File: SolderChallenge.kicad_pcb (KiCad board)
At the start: 2 copper layers, 50 x 100 mm, 41 parts, among them Q1 MOS_N, Q2 MOS_N, Q3 MOS_N, Q4 MOS_N_x2, U1 555, U2 555, U3 555

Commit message: Add name, rev and github URL to back silkscreen
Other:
- board text added: "Iain Chalmers V0.2 https://github.com/icchalmers/SolderChallenge"
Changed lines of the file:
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@@
   (general
     (thickness 1.6)
-    (drawings 54)
+    (drawings 55)
     (tracks 255)
     (zones 0)
@@
     )
   )
+  (gr_text "Iain Chalmers\nV0.2\nhttps://github.com/icchalmers/SolderChallenge" (at 74.7 56.2) (layer B.SilkS)
+    (effects (font (size 1.2 1.2) (thickness 0.2)) (justify mirror))
+  )
   (gr_text "Press 9V battery\non pads to display score" (at 54.25 76 90) (layer F.SilkS)

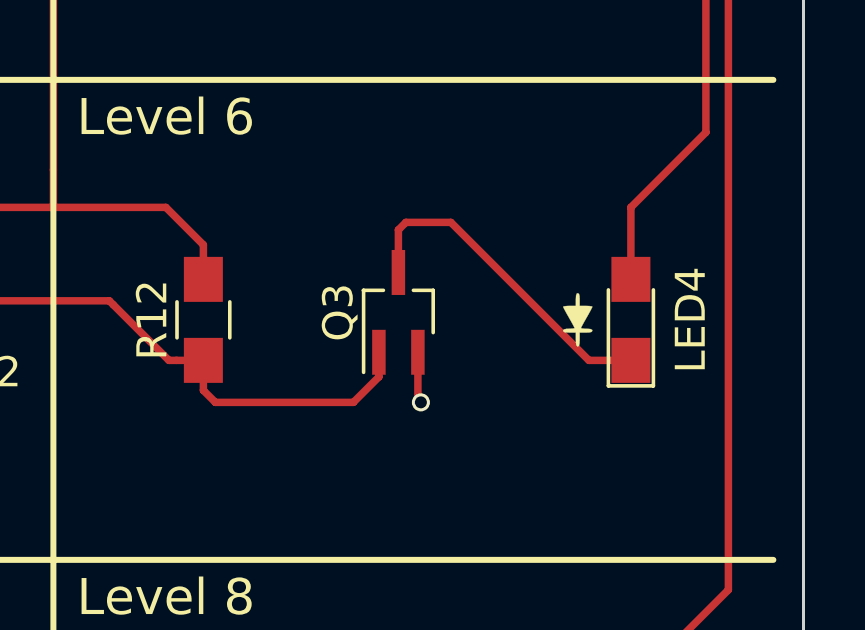
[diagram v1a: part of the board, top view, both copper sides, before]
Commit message: Change Q3 to SOT-23 in place of SOT-323. The difference is that the Q3 footprint uses the recommended solder footprint, whereas Q2 uses the KiCAD hand solder footprint. Should be a good example of using the right footprint depending on the situation
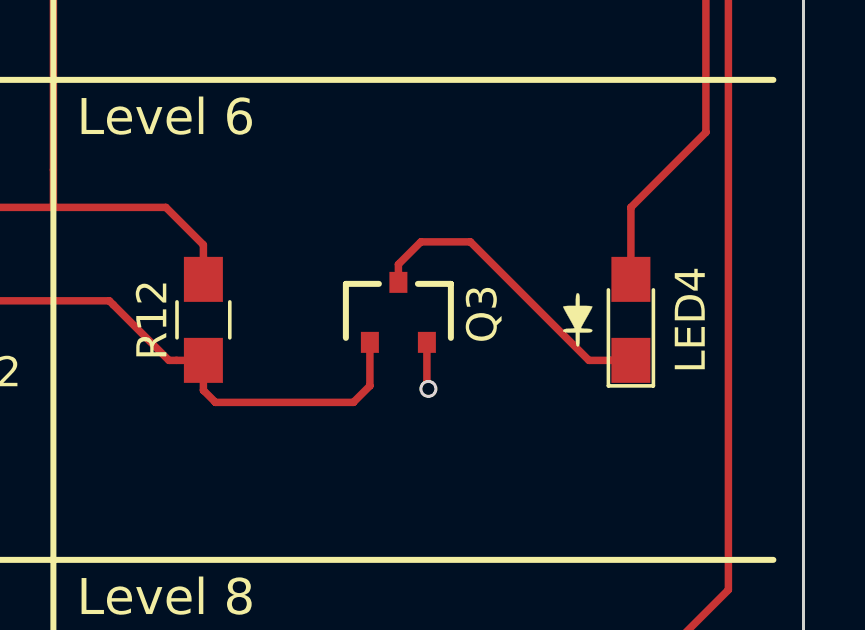
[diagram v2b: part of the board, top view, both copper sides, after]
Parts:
- Q3: footprint SolderChallenge:SOT-323_SC-70_GSD_Handsoldering -> SolderChallenge:SOT-23_GSD_Nexperia_TO-236AB
- turned Q3 to 180 degrees
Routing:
- net Net-(LED4-Pad1): track 11.2 -> 10.3 mm
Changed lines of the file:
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@@
     (add_net VCC)
+  )
+  (module SolderChallenge:SOT-23_GSD_Nexperia_TO-236AB (layer F.Cu)
+    (at 86.5 115.75 180)
+    (descr "SOT-23, Standard")
+    (tags SOT-23)
+    (attr smd)
+    (fp_text reference Q3 (at -2.8 -0.05 90) (layer F.SilkS)
+      (effects (font (size 1 1) (thickness 0.15)))
+    )
+    (fp_text value MOS_N (at 0 2.5 180) (layer F.Fab)
+      (effects (font (size 1 1) (thickness 0.15)))
+    )
+    (fp_line (start 1.45 -0.85) (end 1.65 -0.85) (layer F.CrtYd) (width 0.2))
+    (fp_line (start 1.45 -1.5) (end 1.45 -0.85) (layer F.CrtYd) (width 0.2))
+    (fp_line (start -1.45 -0.85) (end -1.65 -0.85) (layer F.CrtYd) (width 0.2))
+    (fp_line (start -1.45 -1.5) (end -1.45 -0.85) (layer F.CrtYd) (width 0.2))
+    (fp_line (start -1.65 0.85) (end 1.65 0.85) (layer F.CrtYd) (width 0.2))
+    (fp_line (start 1.65 -0.85) (end 1.65 0.85) (layer F.CrtYd) (width 0.2))
+    (fp_line (start -1.45 -1.5) (end 1.45 -1.5) (layer F.CrtYd) (width 0.2))
+    (fp_line (start -1.65 -0.85) (end -1.65 0.85) (layer F.CrtYd) (width 0.2))
+    (fp_line (start 1.75 0.95) (end 0.65 0.95) (layer F.SilkS) (width 0.2))
+    (fp_line (start 1.75 -0.85) (end 1.75 0.95) (layer F.SilkS) (width 0.2))
+    (fp_line (start -1.75 0.95) (end -0.65 0.95) (layer F.SilkS) (width 0.2))
+    (fp_line (start -1.75 -0.85) (end -1.75 0.95) (layer F.SilkS) (width 0.2))
+    (fp_line (start -1.65 -0.85) (end -1.65 0.85) (layer F.Fab) (width 0.2))
+    (fp_line (start 1.65 -0.25) (end 1.65 0.85) (layer F.Fab) (width 0.2))
+    (fp_line (start -1.65 -0.85) (end 1.1 -0.85) (layer F.Fab) (width 0.2))
+    (fp_line (start -1.65 0.85) (end 1.65 0.85) (layer F.Fab) (width 0.2))
+    (fp_line (start 1.1 -0.85) (end 1.65 -0.25) (layer F.Fab) (width 0.2))
+    (pad D smd rect (at 0 1 180) (size 0.6 0.7) (layers F.Cu F.Paste F.Mask)
+      (net 12 "Net-(LED4-Pad1)") (solder_mask_margin 0.05) (solder_paste_margin -0.05))
+    (pad G smd rect (at 0.95 -1 180) (size 0.6 0.7) (layers F.Cu F.Paste F.Mask)
+      (net 22 "Net-(Q3-PadG)") (solder_mask_margin 0.05) (solder_paste_margin -0.05))
+    (pad S smd rect (at -0.95 -1 180) (size 0.6 0.7) (layers F.Cu F.Paste F.Mask)
+      (net 2 GND) (solder_mask_margin 0.05) (solder_paste_margin -0.05))
+    (model TO_SOT_Packages_SMD.3dshapes/SOT-23.wrl
+      (at (xyz 0 0 0))
+      (scale (xyz 1 1 1))
+      (rotate (xyz 0 0 90))
+    )
   )
   (module SolderChallenge:TSSOP-8_4.4x3mm_Pitch0.65mm (layer F.Cu)
@@
       (xy 15.738353 -1.07461)) (layer F.Mask) (width 0.01))
   )
-  (module SolderChallenge:SOT-323_SC-70_GSD_Handsoldering (layer F.Cu)
-    (at 86.5 115.75 90)
-    (descr "SOT-323, SC-70 Handsoldering")
-    (tags "SOT-323 SC-70 Handsoldering")
-    (attr smd)
-    (fp_text reference Q3 (at 0 -2 90) (layer F.SilkS)
-      (effects (font (size 1 1) (thickness 0.15)))
-    )
-    (fp_text value MOS_N (at 0 2.05 90) (layer F.Fab) hide
-      (effects (font (size 1 1) (thickness 0.15)))
-    )
-    (fp_text user %R (at 0 0 180) (layer F.Fab)
-      (effects (font (size 0.5 0.5) (thickness 0.075)))
-    )
-    (fp_line (start 0.735 0.5) (end 0.735 1.16) (layer F.SilkS) (width 0.12))
-    (fp_line (start 0.735 -1.17) (end 0.735 -0.5) (layer F.SilkS) (width 0.12))
-    (fp_line (start 2.4 1.3) (end -2.4 1.3) (layer F.CrtYd) (width 0.05))
-    (fp_line (start 2.4 -1.3) (end 2.4 1.3) (layer F.CrtYd) (width 0.05))
-    (fp_line (start -2.4 -1.3) (end 2.4 -1.3) (layer F.CrtYd) (width 0.05))
-    (fp_line (start -2.4 1.3) (end -2.4 -1.3) (layer F.CrtYd) (width 0.05))
-    (fp_line (start 0.735 -1.16) (end -2 -1.16) (layer F.SilkS) (width 0.12))
-    (fp_line (start -0.675 1.16) (end 0.735 1.16) (layer F.SilkS) (width 0.12))
-    (fp_line (start 0.675 -1.1) (end -0.175 -1.1) (layer F.Fab) (width 0.1))
-    (fp_line (start -0.675 -0.6) (end -0.675 1.1) (layer F.Fab) (width 0.1))
-    (fp_line (start 0.675 -1.1) (end 0.675 1.1) (layer F.Fab) (width 0.1))
-    (fp_line (start 0.675 1.1) (end -0.675 1.1) (layer F.Fab) (width 0.1))
-    (fp_line (start -0.175 -1.1) (end -0.675 -0.6) (layer F.Fab) (width 0.1))
-    (pad G smd rect (at -1.33 -0.65) (size 0.45 1.5) (layers F.Cu F.Paste F.Mask)
-      (net 22 "Net-(Q3-PadG)"))
-    (pad S smd rect (at -1.33 0.65) (size 0.45 1.5) (layers F.Cu F.Paste F.Mask)
-      (net 2 GND))
-    (pad D smd rect (at 1.33 0) (size 0.45 1.5) (layers F.Cu F.Paste F.Mask)
-      (net 12 "Net-(LED4-Pad1)"))
-    (model ${KISYS3DMOD}/TO_SOT_Packages_SMD.3dshapes/SOT-323_SC-70.wrl
-      (at (xyz 0 0 0))
-      (scale (xyz 1 1 1))
-      (rotate (xyz 0 0 0))
-    )
-  )
   (module SolderChallenge:SOT-23_GSD_Handsoldering (layer F.Cu)
     (at 87.075 100 90)
@@
   (segment (start 71.655 117.905) (end 72 118.25) (width 0.25) (layer F.Cu) (net 2))
   (segment (start 72 118.25) (end 72 118.75) (width 0.25) (layer F.Cu) (net 2))
-  (segment (start 87.15 117.08) (end 87.15 118.65) (width 0.25) (layer F.Cu) (net 2))
-  (segment (start 87.15 118.65) (end 87.25 118.75) (width 0.25) (layer F.Cu) (net 2))
-  (via (at 87.25 118.75) (size 0.6) (drill 0.4) (layers F.Cu B.Cu) (net 2))
   (segment (start 70.95 132.975) (end 71.975 132.975) (width 0.25) (layer F.Cu) (net 2))
   (segment (start 71.975 132.975) (end 72.5 133.5) (width 0.25) (layer F.Cu) (net 2))
@@
   (segment (start 88.025 103.225) (end 88 103.25) (width 0.25) (layer F.Cu) (net 2))
   (via (at 88 103.25) (size 0.6) (drill 0.4) (layers F.Cu B.Cu) (net 2))
+  (via (at 87.5 118.3) (size 0.6) (drill 0.4) (layers F.Cu B.Cu) (net 2))
+  (segment (start 87.45 116.75) (end 87.45 118.25) (width 0.25) (layer F.Cu) (net 2))
+  (segment (start 87.45 118.25) (end 87.5 118.3) (width 0.25) (layer F.Cu) (net 2))
   (segment (start 59.08 98.72) (end 61.62 101.26) (width 0.25) (layer B.Cu) (net 3))
   (segment (start 61.62 101.26) (end 66.7 101.26) (width 0.25) (layer B.Cu) (net 3))
@@
   (via (at 94.25 96.25) (size 0.6) (drill 0.4) (layers F.Cu B.Cu) (net 11))
   (segment (start 76.38 77.5) (end 76.38 83.88) (width 0.25) (layer B.Cu) (net 11))
-  (segment (start 86.5 114.42) (end 86.5 113) (width 0.25) (layer F.Cu) (net 12))
-  (segment (start 86.5 113) (end 86.75 112.75) (width 0.25) (layer F.Cu) (net 12))
-  (segment (start 86.75 112.75) (end 88.25 112.75) (width 0.25) (layer F.Cu) (net 12))
-  (segment (start 88.25 112.75) (end 92.85 117.35) (width 0.25) (layer F.Cu) (net 12))
   (segment (start 92.85 117.35) (end 94.25 117.35) (width 0.25) (layer F.Cu) (net 12))
+  (segment (start 88.9 113.4) (end 92.85 117.35) (width 0.25) (layer F.Cu) (net 12))
+  (segment (start 87.25 113.4) (end 88.9 113.4) (width 0.25) (layer F.Cu) (net 12))
+  (segment (start 86.5 114.15) (end 87.25 113.4) (width 0.25) (layer F.Cu) (net 12))
+  (segment (start 86.5 114.75) (end 86.5 114.15) (width 0.25) (layer F.Cu) (net 12))
   (segment (start 98 73.5) (end 98 74.75) (width 0.25) (layer F.Cu) (net 13))
   (segment (start 98 74.75) (end 96.75 76) (width 0.25) (layer F.Cu) (net 13))
@@
   (segment (start 80.4 118.75) (end 85 118.75) (width 0.25) (layer F.Cu) (net 22))
   (segment (start 80 118.35) (end 80.4 118.75) (width 0.25) (layer F.Cu) (net 22))
-  (segment (start 85 118.75) (end 85.85 117.9) (width 0.25) (layer F.Cu) (net 22))
-  (segment (start 85.85 117.9) (end 85.85 117.08) (width 0.25) (layer F.Cu) (net 22))
   (segment (start 77 115.5) (end 78.85 117.35) (width 0.25) (layer F.Cu) (net 22))
   (segment (start 78.85 117.35) (end 79.1 117.35) (width 0.25) (layer F.Cu) (net 22))
   (segment (start 79.1 117.35) (end 80 117.35) (width 0.25) (layer F.Cu) (net 22))
+  (segment (start 85.55 118.2) (end 85 118.75) (width 0.25) (layer F.Cu) (net 22))
+  (segment (start 85.55 116.75) (end 85.55 118.2) (width 0.25) (layer F.Cu) (net 22))
   (segment (start 58.25 133.35) (end 61.75 133.35) (width 0.25) (layer F.Cu) (net 23))
   (segment (start 61.75 133.35) (end 62.65 133.35) (width 0.25) (layer F.Cu) (net 23))

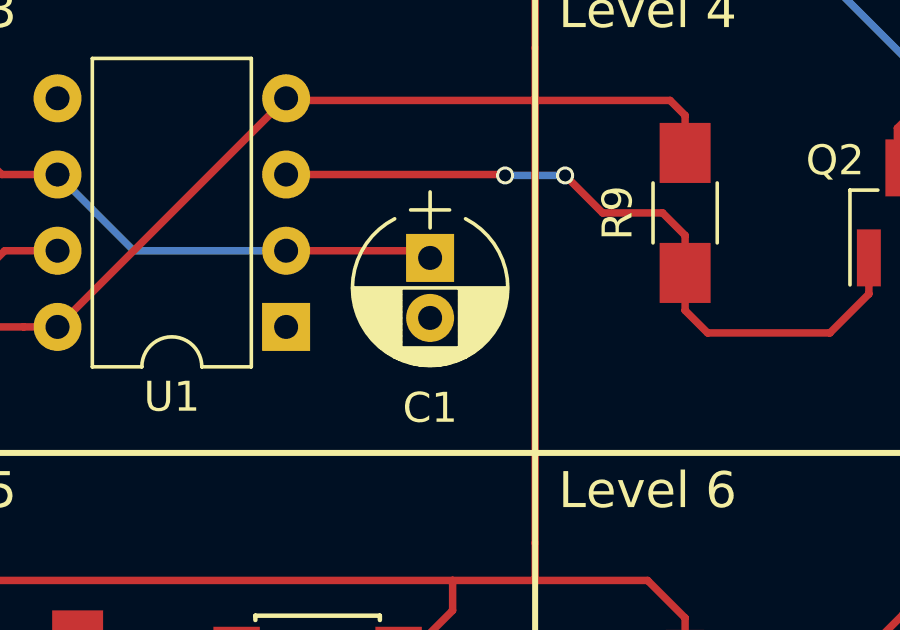
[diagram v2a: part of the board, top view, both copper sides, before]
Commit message: Change C1 to non polarised. Pops would have been fun if people soldered it in round the wrong way, but health and safety prevails over fun :(
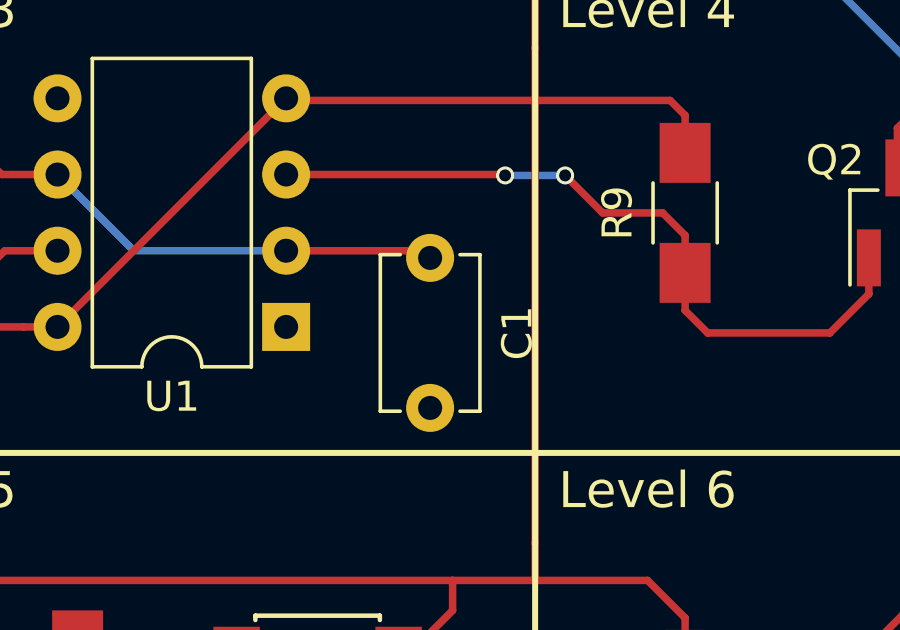
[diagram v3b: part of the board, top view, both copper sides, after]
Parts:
- C1: footprint SolderChallenge:CP_Radial_D5.0mm_P2.00mm -> SolderChallenge:C_Disc_D5.1mm_W3.2mm_P5.00mm

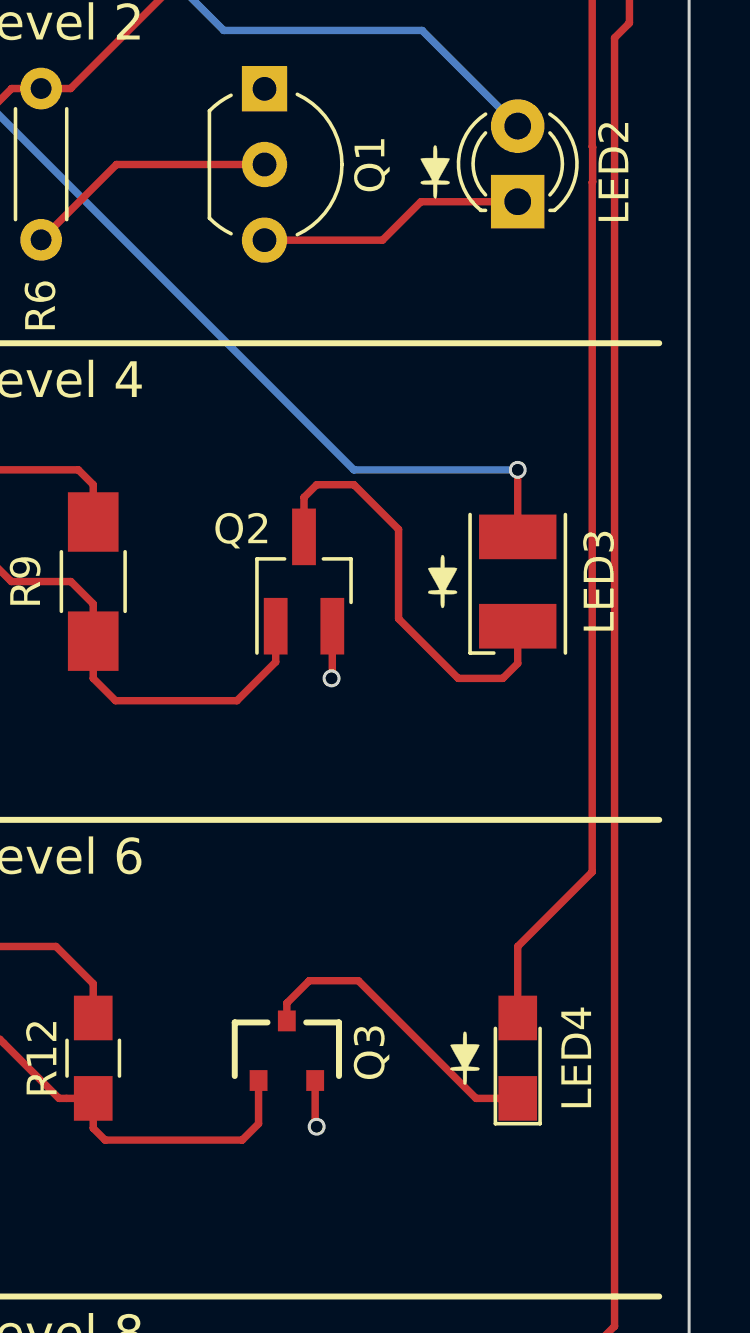
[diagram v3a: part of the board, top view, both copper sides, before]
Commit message: Switch orientation of one LED to force people to think about orientation. This is to make people more orientation aware without risking an exploding electrolytic in the face
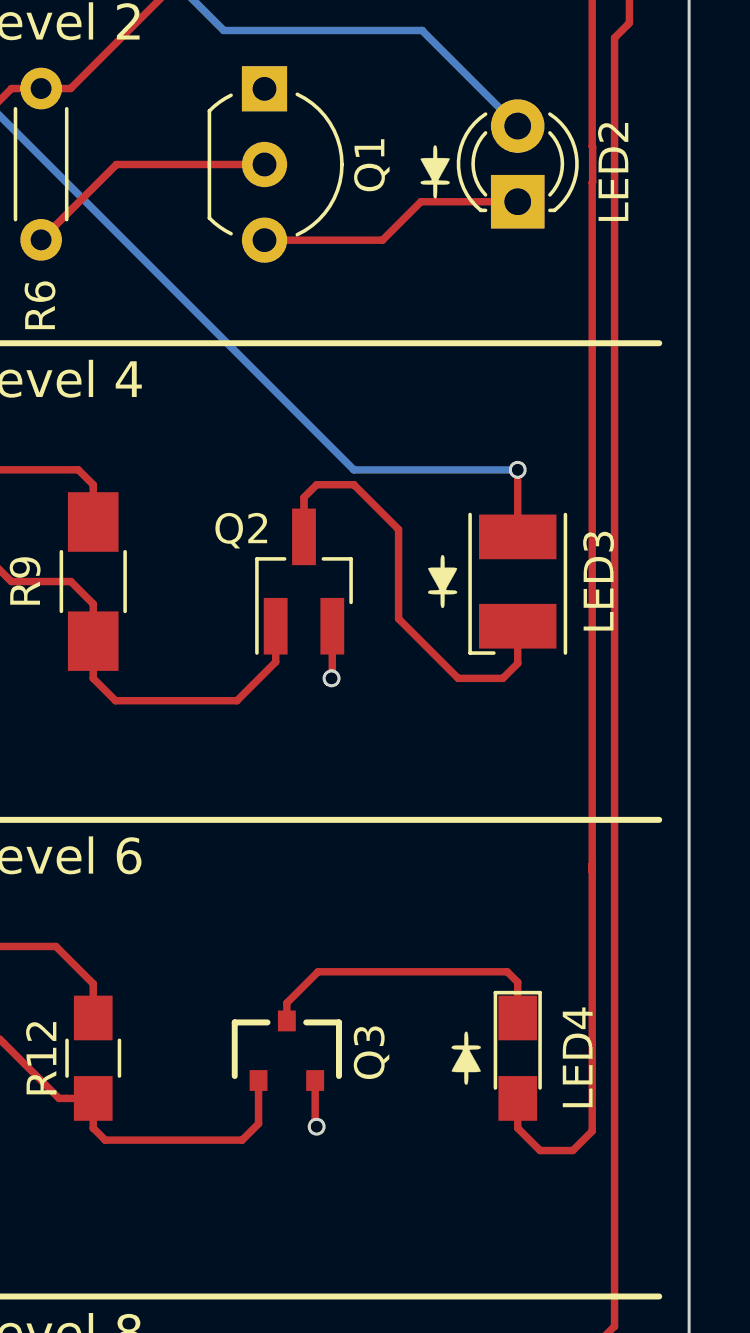
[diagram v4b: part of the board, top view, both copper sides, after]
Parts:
- turned G*** to 90 degrees
- turned LED4 to 270 degrees
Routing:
- net LED4_Vcc: track 42.7 -> 49.8 mm
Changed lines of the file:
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@@
     (thickness 1.6)
     (drawings 55)
-    (tracks 255)
+    (tracks 259)
     (zones 0)
     (modules 41)
@@
   )
   (module SolderChallenge:0803_diode_silk (layer F.Cu)
-    (at 92.5 116 270)
-    (fp_text reference G*** (at 0 0 270) (layer F.SilkS) hide
+    (at 92.5 116 90)
+    (fp_text reference G*** (at 0 0 90) (layer F.SilkS) hide
       (effects (font (size 1.524 1.524) (thickness 0.3)))
     )
-    (fp_text value LOGO (at 0.75 0 270) (layer F.SilkS) hide
+    (fp_text value LOGO (at 0.75 0 90) (layer F.SilkS) hide
       (effects (font (size 1.524 1.524) (thickness 0.3)))
     )
@@
   )
   (module SolderChallenge:LED_0805_HandSoldering (layer F.Cu)
-    (at 94.25 116 90)
+    (at 94.25 116 270)
     (descr "Resistor SMD 0805, hand soldering")
     (tags "resistor 0805")
     (attr smd)
-    (fp_text reference LED4 (at 0 2 90) (layer F.SilkS)
-      (effects (font (size 1 1) (thickness 0.15)))
-    )
-    (fp_text value LED (at 0 1.75 90) (layer F.Fab)
+    (fp_text reference LED4 (at 0 -2.05 270) (layer F.SilkS)
+      (effects (font (size 1 1) (thickness 0.15)))
+    )
+    (fp_text value LED (at 0 1.75 270) (layer F.Fab)
       (effects (font (size 1 1) (thickness 0.15)))
     )
@@
     (fp_line (start 2.35 0.9) (end -2.35 0.9) (layer F.CrtYd) (width 0.05))
     (fp_line (start -2.2 -0.75) (end -2.2 0.75) (layer F.SilkS) (width 0.12))
-    (pad 1 smd rect (at -1.35 0 90) (size 1.5 1.3) (layers F.Cu F.Paste F.Mask)
+    (pad 1 smd rect (at -1.35 0 270) (size 1.5 1.3) (layers F.Cu F.Paste F.Mask)
       (net 12 "Net-(LED4-Pad1)"))
-    (pad 2 smd rect (at 1.35 0 90) (size 1.5 1.3) (layers F.Cu F.Paste F.Mask)
+    (pad 2 smd rect (at 1.35 0 270) (size 1.5 1.3) (layers F.Cu F.Paste F.Mask)
       (net 13 LED4_Vcc))
     (model ${KISYS3DMOD}/LEDs.3dshapes/LED_0805.wrl
@@
   (via (at 94.25 96.25) (size 0.6) (drill 0.4) (layers F.Cu B.Cu) (net 11))
   (segment (start 76.38 77.5) (end 76.38 83.88) (width 0.25) (layer B.Cu) (net 11))
-  (segment (start 92.85 117.35) (end 94.25 117.35) (width 0.25) (layer F.Cu) (net 12))
-  (segment (start 88.9 113.4) (end 92.85 117.35) (width 0.25) (layer F.Cu) (net 12))
-  (segment (start 87.25 113.4) (end 88.9 113.4) (width 0.25) (layer F.Cu) (net 12))
-  (segment (start 86.5 114.15) (end 87.25 113.4) (width 0.25) (layer F.Cu) (net 12))
+  (segment (start 94.25 113.45) (end 94.25 114.65) (width 0.25) (layer F.Cu) (net 12))
+  (segment (start 93.9 113.1) (end 94.25 113.45) (width 0.25) (layer F.Cu) (net 12))
+  (segment (start 87.55 113.1) (end 93.9 113.1) (width 0.25) (layer F.Cu) (net 12))
   (segment (start 86.5 114.75) (end 86.5 114.15) (width 0.25) (layer F.Cu) (net 12))
+  (segment (start 86.5 114.15) (end 87.55 113.1) (width 0.25) (layer F.Cu) (net 12))
   (segment (start 98 73.5) (end 98 74.75) (width 0.25) (layer F.Cu) (net 13))
   (segment (start 98 74.75) (end 96.75 76) (width 0.25) (layer F.Cu) (net 13))
@@
   (segment (start 96.765001 85.411999) (end 96.765001 86.588001) (width 0.25) (layer F.Cu) (net 13))
   (segment (start 96.765001 86.588001) (end 96.75 86.603002) (width 0.25) (layer F.Cu) (net 13))
-  (segment (start 96.75 86.603002) (end 96.75 109.75) (width 0.25) (layer F.Cu) (net 13))
-  (segment (start 96.75 109.75) (end 94.25 112.25) (width 0.25) (layer F.Cu) (net 13))
-  (segment (start 94.25 112.25) (end 94.25 114.65) (width 0.25) (layer F.Cu) (net 13))
+  (segment (start 96.75 86.603002) (end 96.75 109.5) (width 0.25) (layer F.Cu) (net 13))
+  (segment (start 96.75 109.5) (end 96.75 109.75) (width 0.25) (layer F.Cu) (net 13))
+  (segment (start 96.75 118.45) (end 96.75 109.5) (width 0.25) (layer F.Cu) (net 13))
+  (segment (start 96.1 119.1) (end 96.75 118.45) (width 0.25) (layer F.Cu) (net 13))
+  (segment (start 95 119.1) (end 96.1 119.1) (width 0.25) (layer F.Cu) (net 13))
+  (segment (start 94.25 117.35) (end 94.25 118.35) (width 0.25) (layer F.Cu) (net 13))
+  (segment (start 94.25 118.35) (end 95 119.1) (width 0.25) (layer F.Cu) (net 13))
   (segment (start 81.7 131.35) (end 83.6 131.35) (width 0.25) (layer F.Cu) (net 14))
   (segment (start 83.6 131.35) (end 84.25 132) (width 0.25) (layer F.Cu) (net 14))
